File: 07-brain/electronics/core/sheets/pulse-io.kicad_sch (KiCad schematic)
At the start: 0 parts

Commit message: Added audio io to Brain
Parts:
- added Q4, Q5: MMBT3904, Package_TO_SOT_SMD:SOT-23, symbol Transistor_BJT:MMBT3904
- added R33, R34: 100k, Resistor_SMD:R_0603_1608Metric, symbol Device:R
- added R35: 10k, Resistor_SMD:R_0603_1608Metric, symbol Device:R
- added R36: 7.5k, Resistor_SMD:R_0603_1608Metric, symbol Device:R
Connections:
- new net: Q5.1 (B), R34.2
- new net: Q4.1 (B), R33.2
- new net +12V: R35.2
- new net GND: Q4.2 (E), Q5.2 (E), R36.1
- new net GPIO_PULSE_IN: Q4.3 (C)
- new net GPIO_PULSE_OUT: R34.1
- new net PULSE_IN: R33.1
- new net PULSE_OUT: Q5.3 (C), R35.1, R36.2
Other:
- note added: "About 5.1V pulses"
- note added: "Pulse is inverted. Since the input is inverted too, if you just want to let pulses through you don't need to invert anything."
- note added: "Use Pico's pull up resistor to set value to logical 1. On pulse in, it goes to 0."

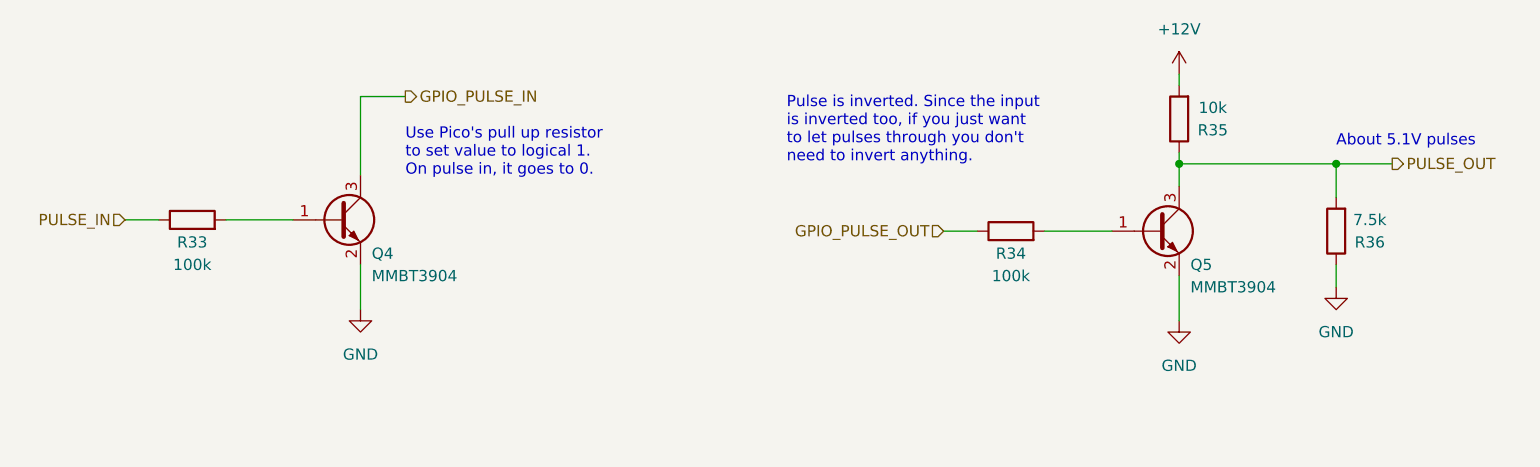
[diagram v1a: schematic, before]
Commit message: Added pulse component and tests to Brain
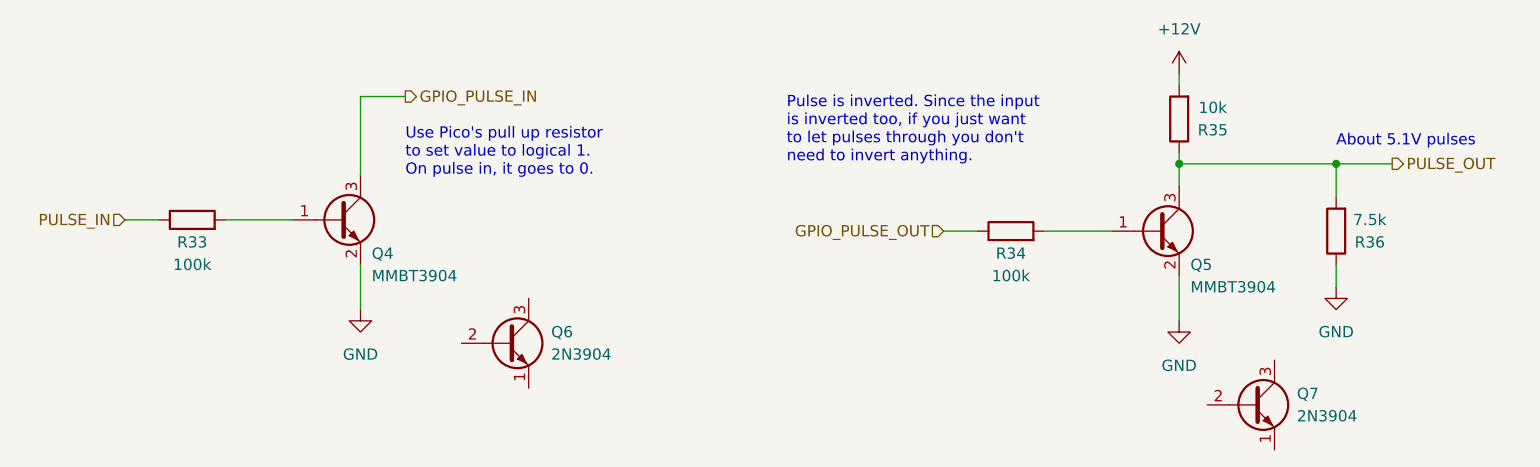
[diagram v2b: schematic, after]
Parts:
- added Q6, Q7: 2N3904, Package_TO_SOT_THT:TO-92_Inline, symbol Transistor_BJT:2N3904
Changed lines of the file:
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@@
+	)
+	(symbol
+		(lib_id "Transistor_BJT:2N3904")
+		(at 115.57 100.33 0)
+		(unit 1)
+		(exclude_from_sim no)
+		(in_bom yes)
+		(on_board yes)
+		(dnp no)
+		(fields_autoplaced yes)
+		(property "Reference" "Q6"
+			(at 120.65 99.0599 0)
+			(effects
+				(font
+					(size 1.27 1.27)
+				)
+				(justify left)
+			)
+		)
+		(property "Value" "2N3904"
+			(at 120.65 101.5999 0)
+			(effects
+				(font
+					(size 1.27 1.27)
+				)
+				(justify left)
+			)
+		)
+		(property "Footprint" "Package_TO_SOT_THT:TO-92_Inline"
+			(at 120.65 102.235 0)
+			(effects
+				(font
+					(size 1.27 1.27)
+					(italic yes)
+				)
+				(justify left)
+				(hide yes)
+			)
+		)
+		(property "Datasheet" "https://www.onsemi.com/pub/Collateral/2N3903-D.PDF"
+			(at 115.57 100.33 0)
+			(effects
+				(font
+					(size 1.27 1.27)
+				)
+				(justify left)
+				(hide yes)
+			)
+		)
+		(property "Description" "0.2A Ic, 40V Vce, Small Signal NPN Transistor, TO-92"
+			(at 115.57 100.33 0)
+			(effects
+				(font
+					(size 1.27 1.27)
+				)
+				(hide yes)
+			)
+		)
+		(pin "2"
+		)
+		(pin "3"
+		)
+		(pin "1"
+		)
+		(instances
+			(project ""
+				(path "/8e2e31f3-eed5-4de1-966c-f4162758c735/b082d257-9358-41e3-a203-3f08ae6b6f5f"
+					(reference "Q6")
+					(unit 1)
+				)
+			)
+		)
 	)
 	(symbol
@@
 					(unit 1)
 				)
+			)
+		)
+	)
+	(symbol
+		(lib_id "Transistor_BJT:2N3904")
+		(at 200.025 107.315 0)
+		(unit 1)
+		(exclude_from_sim no)
+		(in_bom yes)
+		(on_board yes)
+		(dnp no)
+		(fields_autoplaced yes)
+		(property "Reference" "Q7"
+			(at 205.105 106.0449 0)
+			(effects
+				(font
+					(size 1.27 1.27)
+				)
+				(justify left)
+			)
+		)
+		(property "Value" "2N3904"
+			(at 205.105 108.5849 0)
+			(effects
+				(font
+					(size 1.27 1.27)
+				)
+				(justify left)
+			)
+		)
+		(property "Footprint" "Package_TO_SOT_THT:TO-92_Inline"
+			(at 205.105 109.22 0)
+			(effects
+				(font
+					(size 1.27 1.27)
+					(italic yes)
+				)
+				(justify left)
+				(hide yes)
+			)
+		)
+		(property "Datasheet" "https://www.onsemi.com/pub/Collateral/2N3903-D.PDF"
+			(at 200.025 107.315 0)
+			(effects
+				(font
+					(size 1.27 1.27)
+				)
+				(justify left)
+				(hide yes)
+			)
+		)
+		(property "Description" "0.2A Ic, 40V Vce, Small Signal NPN Transistor, TO-92"
+			(at 200.025 107.315 0)
+			(effects
+				(font
+					(size 1.27 1.27)
+				)
+				(hide yes)
+			)
+		)
+		(pin "2"
+		)
+		(pin "3"
+		)
+		(pin "1"
+		)
+		(instances
+			(project "brain-core"
+				(path "/8e2e31f3-eed5-4de1-966c-f4162758c735/b082d257-9358-41e3-a203-3f08ae6b6f5f"
+					(reference "Q7")
+					(unit 1)
+				)

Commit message: Audio/CV out BrainSDK tested/working
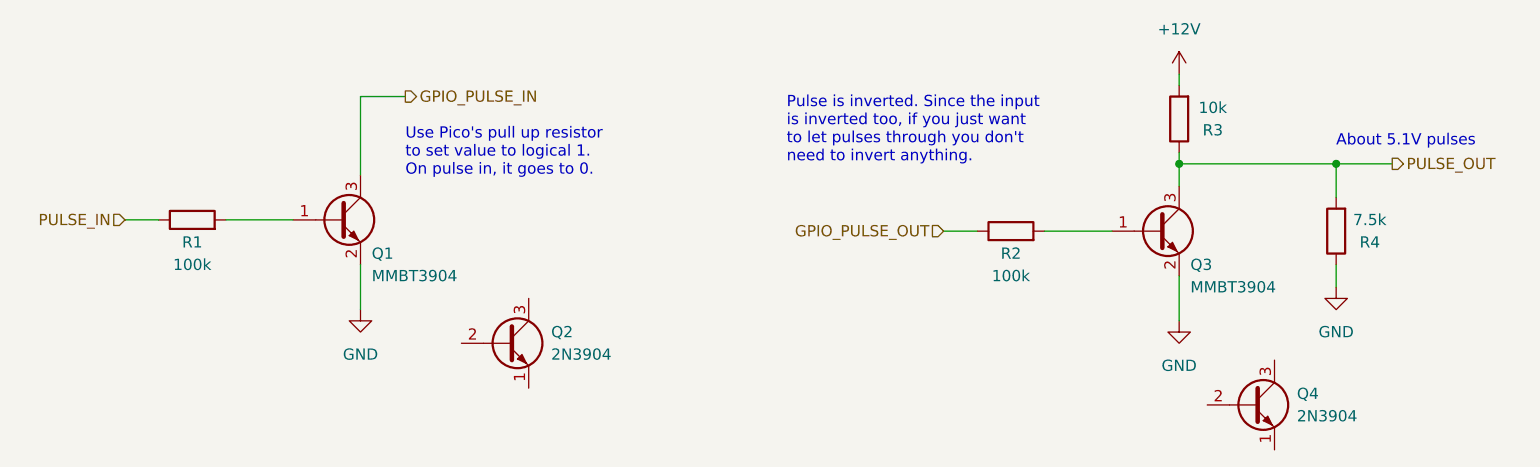
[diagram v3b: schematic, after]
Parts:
- renumbered Q4 to Q1, Q6 to Q2, Q5 to Q3, Q7 to Q4, R33 to R1, R34 to R2, R35 to R3, R36 to R4
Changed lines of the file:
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@@
 		(dnp no)
 		(fields_autoplaced yes)
-		(property "Reference" "#PWR051"
+		(property "Reference" "#PWR023"
 			(at 191.77 73.66 0)
 			(effects
@@
 			(project ""
 				(path "/8e2e31f3-eed5-4de1-966c-f4162758c735/b082d257-9358-41e3-a203-3f08ae6b6f5f"
-					(reference "#PWR051")
+					(reference "#PWR023")
 					(unit 1)
 				)
@@
 		(on_board yes)
 		(dnp no)
-		(property "Reference" "R35"
+		(property "Reference" "R3"
 			(at 195.58 76.2 0)
 			(effects
@@
 			(project "brain-core"
 				(path "/8e2e31f3-eed5-4de1-966c-f4162758c735/b082d257-9358-41e3-a203-3f08ae6b6f5f"
-					(reference "R35")
+					(reference "R3")
 					(unit 1)
 				)
@@
 		(dnp no)
 		(fields_autoplaced yes)
-		(property "Reference" "#PWR049"
+		(property "Reference" "#PWR022"
 			(at 99.06 102.87 0)
 			(effects
@@
 			(project ""
 				(path "/8e2e31f3-eed5-4de1-966c-f4162758c735/b082d257-9358-41e3-a203-3f08ae6b6f5f"
-					(reference "#PWR049")
+					(reference "#PWR022")
 					(unit 1)
 				)
@@
 		(on_board yes)
 		(dnp no)
-		(property "Reference" "Q5"
+		(property "Reference" "Q3"
 			(at 193.04 91.44 0)
 			(effects
@@
 			(project "brain-core"
 				(path "/8e2e31f3-eed5-4de1-966c-f4162758c735/b082d257-9358-41e3-a203-3f08ae6b6f5f"
-					(reference "Q5")
+					(reference "Q3")
 					(unit 1)
 				)
@@
 		(dnp no)
 		(fields_autoplaced yes)
-		(property "Reference" "#PWR052"
+		(property "Reference" "#PWR025"
 			(at 209.55 100.33 0)
 			(effects
@@
 			(project "brain-core"
 				(path "/8e2e31f3-eed5-4de1-966c-f4162758c735/b082d257-9358-41e3-a203-3f08ae6b6f5f"
-					(reference "#PWR052")
+					(reference "#PWR025")
 					(unit 1)
 				)
@@
 		(on_board yes)
 		(dnp no)
-		(property "Reference" "R34"
+		(property "Reference" "R2"
 			(at 172.72 90.17 90)
 			(effects
@@
 			(project "brain-core"
 				(path "/8e2e31f3-eed5-4de1-966c-f4162758c735/b082d257-9358-41e3-a203-3f08ae6b6f5f"
-					(reference "R34")
+					(reference "R2")
 					(unit 1)
 				)
@@
 		(dnp no)
 		(fields_autoplaced yes)
-		(property "Reference" "Q6"
+		(property "Reference" "Q2"
 			(at 120.65 99.0599 0)
 			(effects
@@
 			(project ""
 				(path "/8e2e31f3-eed5-4de1-966c-f4162758c735/b082d257-9358-41e3-a203-3f08ae6b6f5f"
-					(reference "Q6")
+					(reference "Q2")
 					(unit 1)
 				)
@@
 		(on_board yes)
 		(dnp no)
-		(property "Reference" "R36"
+		(property "Reference" "R4"
 			(at 213.36 88.9 0)
 			(effects
@@
 			(project "brain-core"
 				(path "/8e2e31f3-eed5-4de1-966c-f4162758c735/b082d257-9358-41e3-a203-3f08ae6b6f5f"
-					(reference "R36")
+					(reference "R4")
 					(unit 1)
 				)
@@
 		(dnp no)
 		(fields_autoplaced yes)
-		(property "Reference" "#PWR050"
+		(property "Reference" "#PWR024"
 			(at 191.77 104.14 0)
 			(effects
@@
 			(project "brain-core"
 				(path "/8e2e31f3-eed5-4de1-966c-f4162758c735/b082d257-9358-41e3-a203-3f08ae6b6f5f"
-					(reference "#PWR050")
+					(reference "#PWR024")
 					(unit 1)
 				)
@@
 		(dnp no)
 		(fields_autoplaced yes)
-		(property "Reference" "Q7"
+		(property "Reference" "Q4"
 			(at 205.105 106.0449 0)
 			(effects
@@
 			(project "brain-core"
 				(path "/8e2e31f3-eed5-4de1-966c-f4162758c735/b082d257-9358-41e3-a203-3f08ae6b6f5f"
-					(reference "Q7")
+					(reference "Q4")
 					(unit 1)
 				)
@@
 		(on_board yes)
 		(dnp no)
-		(property "Reference" "R33"
+		(property "Reference" "R1"
 			(at 80.01 88.9 90)
 			(effects
@@
 			(project "brain-core"
 				(path "/8e2e31f3-eed5-4de1-966c-f4162758c735/b082d257-9358-41e3-a203-3f08ae6b6f5f"
-					(reference "R33")
+					(reference "R1")
 					(unit 1)
 				)
@@
 		(on_board yes)
 		(dnp no)
-		(property "Reference" "Q4"
+		(property "Reference" "Q1"
 			(at 100.33 90.17 0)
 			(effects
@@
 			(project "brain-core"
 				(path "/8e2e31f3-eed5-4de1-966c-f4162758c735/b082d257-9358-41e3-a203-3f08ae6b6f5f"
-					(reference "Q4")
-					(unit 1)
-				)
+					(reference "Q1")
+					(unit 1)
+				)

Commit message: Design Brain/Core PCB
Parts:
- removed Q2, Q4: 2N3904, Package_TO_SOT_THT:TO-92_Inline, symbol Transistor_BJT:2N3904
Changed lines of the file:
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@@
-	)
-	(symbol
-		(lib_id "Transistor_BJT:2N3904")
-		(at 115.57 100.33 0)
-		(unit 1)
-		(exclude_from_sim no)
-		(in_bom yes)
-		(on_board yes)
-		(dnp no)
-		(fields_autoplaced yes)
-		(property "Reference" "Q2"
-			(at 120.65 99.0599 0)
-			(effects
-				(font
-					(size 1.27 1.27)
-				)
-				(justify left)
-			)
-		)
-		(property "Value" "2N3904"
-			(at 120.65 101.5999 0)
-			(effects
-				(font
-					(size 1.27 1.27)
-				)
-				(justify left)
-			)
-		)
-		(property "Footprint" "Package_TO_SOT_THT:TO-92_Inline"
-			(at 120.65 102.235 0)
-			(effects
-				(font
-					(size 1.27 1.27)
-					(italic yes)
-				)
-				(justify left)
-				(hide yes)
-			)
-		)
-		(property "Datasheet" "https://www.onsemi.com/pub/Collateral/2N3903-D.PDF"
-			(at 115.57 100.33 0)
-			(effects
-				(font
-					(size 1.27 1.27)
-				)
-				(justify left)
-				(hide yes)
-			)
-		)
-		(property "Description" "0.2A Ic, 40V Vce, Small Signal NPN Transistor, TO-92"
-			(at 115.57 100.33 0)
-			(effects
-				(font
-					(size 1.27 1.27)
-				)
-				(hide yes)
-			)
-		)
-		(pin "2"
-		)
-		(pin "3"
-		)
-		(pin "1"
-		)
-		(instances
-			(project ""
-				(path "/8e2e31f3-eed5-4de1-966c-f4162758c735/b082d257-9358-41e3-a203-3f08ae6b6f5f"
-					(reference "Q2")
-					(unit 1)
-				)
-			)
-		)
 	)
 	(symbol
@@
 					(unit 1)
 				)
-			)
-		)
-	)
-	(symbol
-		(lib_id "Transistor_BJT:2N3904")
-		(at 200.025 107.315 0)
-		(unit 1)
-		(exclude_from_sim no)
-		(in_bom yes)
-		(on_board yes)
-		(dnp no)
-		(fields_autoplaced yes)
-		(property "Reference" "Q4"
-			(at 205.105 106.0449 0)
-			(effects
-				(font
-					(size 1.27 1.27)
-				)
-				(justify left)
-			)
-		)
-		(property "Value" "2N3904"
-			(at 205.105 108.5849 0)
-			(effects
-				(font
-					(size 1.27 1.27)
-				)
-				(justify left)
-			)
-		)
-		(property "Footprint" "Package_TO_SOT_THT:TO-92_Inline"
-			(at 205.105 109.22 0)
-			(effects
-				(font
-					(size 1.27 1.27)
-					(italic yes)
-				)
-				(justify left)
-				(hide yes)
-			)
-		)
-		(property "Datasheet" "https://www.onsemi.com/pub/Collateral/2N3903-D.PDF"
-			(at 200.025 107.315 0)
-			(effects
-				(font
-					(size 1.27 1.27)
-				)
-				(justify left)
-				(hide yes)
-			)
-		)
-		(property "Description" "0.2A Ic, 40V Vce, Small Signal NPN Transistor, TO-92"
-			(at 200.025 107.315 0)
-			(effects
-				(font
-					(size 1.27 1.27)
-				)
-				(hide yes)
-			)
-		)
-		(pin "2"
-		)
-		(pin "3"
-		)
-		(pin "1"
-		)
-		(instances
-			(project "brain-core"
-				(path "/8e2e31f3-eed5-4de1-966c-f4162758c735/b082d257-9358-41e3-a203-3f08ae6b6f5f"
-					(reference "Q4")
-					(unit 1)
-				)

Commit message: Brain electronics prod ready
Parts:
- Q1, Q3, R1, R2: CHECKED (none) -> YES
- R3: CHECKED (none) -> YES; LCSC (none) -> C25804
- R4: CHECKED (none) -> YES; LCSC (none) -> C23234
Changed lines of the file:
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@@
 			)
 		)
-		(property "LCSC" ""
+		(property "LCSC" "C25804"
 			(at 191.77 74.93 90)
 			(effects
@@
 		)
 		(property "Sim.Pins" ""
+			(at 191.77 74.93 0)
+			(effects
+				(font
+					(size 1.27 1.27)
+				)
+				(hide yes)
+			)
+		)
+		(property "CHECKED" "YES"
 			(at 191.77 74.93 0)
 			(effects
@@
 			)
 		)
+		(property "CHECKED" "YES"
+			(at 189.23 87.63 0)
+			(effects
+				(font
+					(size 1.27 1.27)
+				)
+				(hide yes)
+			)
+		)
 		(pin "2"
 		)
@@
 			)
 		)
+		(property "CHECKED" "YES"
+			(at 172.72 87.63 90)
+			(effects
+				(font
+					(size 1.27 1.27)
+				)
+				(hide yes)
+			)
+		)
 		(pin "1"
 		)
@@
 			)
 		)
-		(property "LCSC" ""
+		(property "LCSC" "C23234"
 			(at 209.55 87.63 90)
 			(effects
@@
 		)
 		(property "Sim.Pins" ""
+			(at 209.55 87.63 0)
+			(effects
+				(font
+					(size 1.27 1.27)
+				)
+				(hide yes)
+			)
+		)
+		(property "CHECKED" "YES"
 			(at 209.55 87.63 0)
 			(effects
@@
 			)
 		)
+		(property "CHECKED" "YES"
+			(at 80.01 86.36 90)
+			(effects
+				(font
+					(size 1.27 1.27)
+				)
+				(hide yes)
+			)
+		)
 		(pin "1"
 		)
@@
 			(at 96.52 86.36 0)
 			(effects
+				(font
+					(size 1.27 1.27)
+				)
+				(hide yes)
+			)
+		)
+		(property "CHECKED" "YES"
+			(at 96.52 86.36 0)
+			(effects

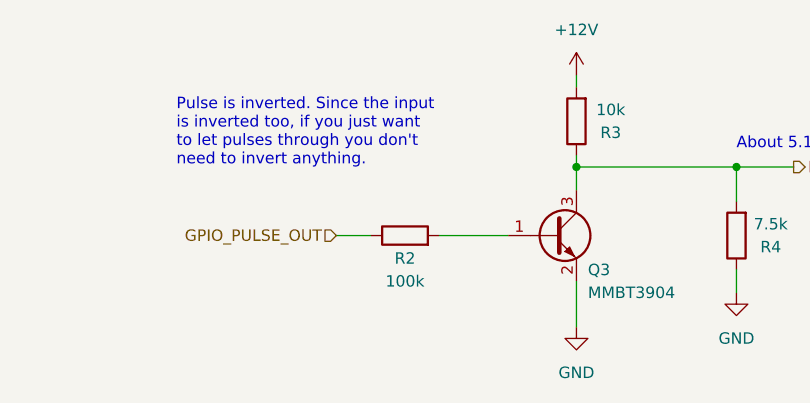
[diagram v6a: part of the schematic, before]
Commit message: Updated LFO LED resistor value
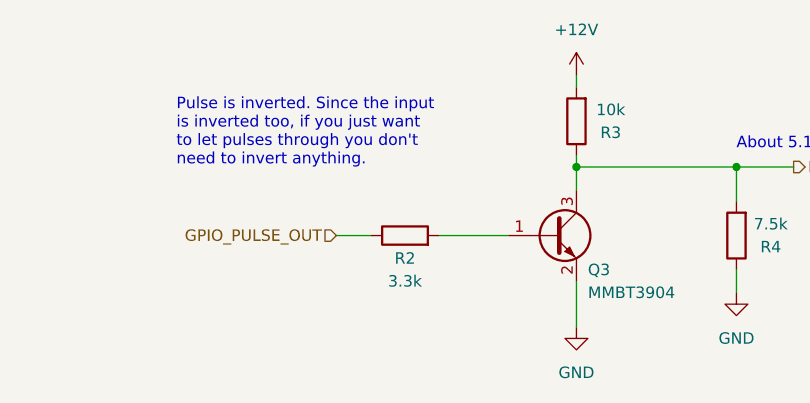
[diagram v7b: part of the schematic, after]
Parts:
- R2: value 100k -> 3.3k; LCSC C25803 -> C22978
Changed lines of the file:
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@@
 			)
 		)
-		(property "Value" "100k"
+		(property "Value" "3.3k"
 			(at 172.72 92.71 90)
 			(effects
@@
 			)
 		)
-		(property "LCSC" "C25803"
+		(property "LCSC" "C22978"
 			(at 172.72 87.63 90)
 			(effects
